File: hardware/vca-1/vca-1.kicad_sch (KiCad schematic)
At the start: 47 parts, among them J1 LIN CV IN, J2 AUDIO IN, J3 OUT, J4 LIN CV IN, J5 AUDIO IN, J6 OUT, J7 Conn_02x05_Odd_Even, Q1 BC557, Q2 BC557, U1 TL074, U2 LM13700

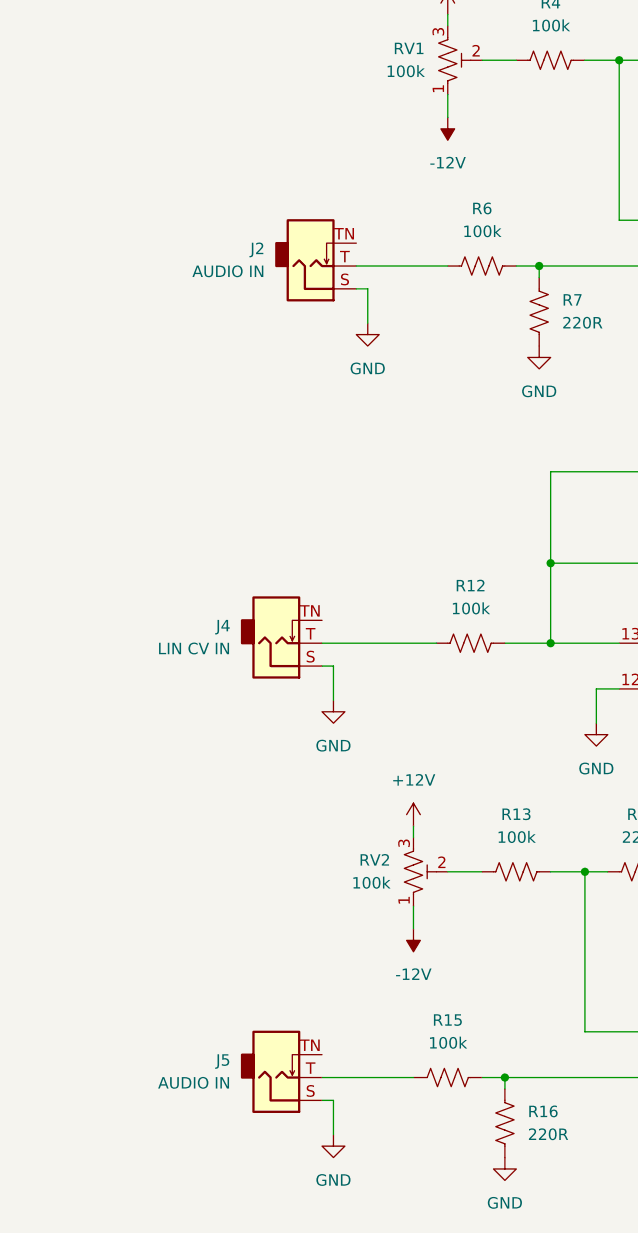
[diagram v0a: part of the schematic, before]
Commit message: Added a level pot on the audio inputs, v1.1
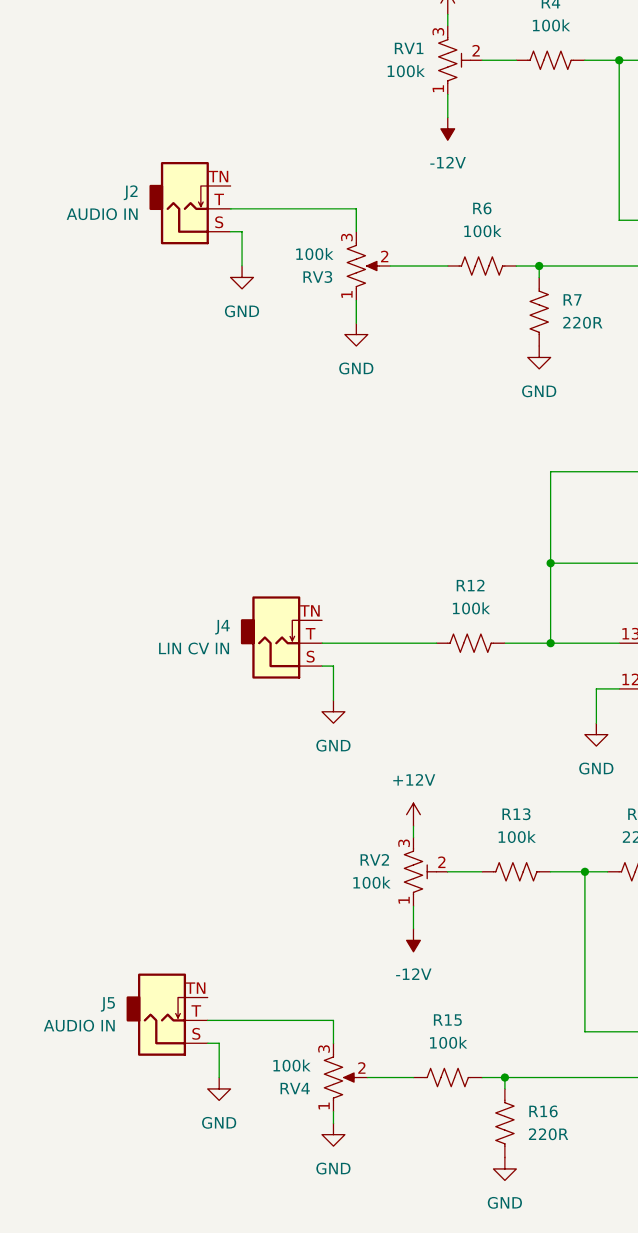
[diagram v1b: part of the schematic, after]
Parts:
- added RV3, RV4: 100k, Potentiometer_THT:Potentiometer_Bourns_PTV09A-2_Single_Horizontal, symbol Device:R_Potentiometer_US
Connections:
- net GND: now also RV3.1, RV4.1
- net at J5.T: now also RV4.3; no longer R15.2
- net at R6.2: now also RV3.2; no longer J2.T
- new net: R15.2, RV4.2
- new net: J2.T, RV3.3
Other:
- moved on the sheet: J2, J5
